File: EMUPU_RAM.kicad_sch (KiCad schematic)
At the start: 22 parts, among them J1 Conn_01x20_Socket, J2 Conn_01x20_Socket, J3 Barrel_Jack_Switch, J4 Conn_01x06_Pin, J5 Conn_01x08_Pin, J6 Conn_01x06_Pin, J7 Conn_01x02_Pin, SW1 SW_SPDT, SW2 SW_SPST, U1 PIC18F57Q43-IPT, U2 HM678127_SOJ32_Arranged

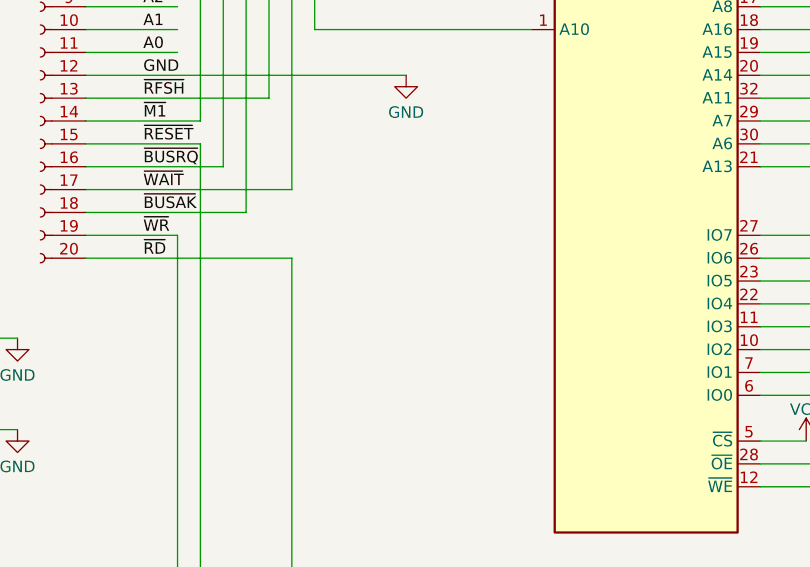
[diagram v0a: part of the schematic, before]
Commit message: Adjusting rule, described in Kosakas book, need some refinements
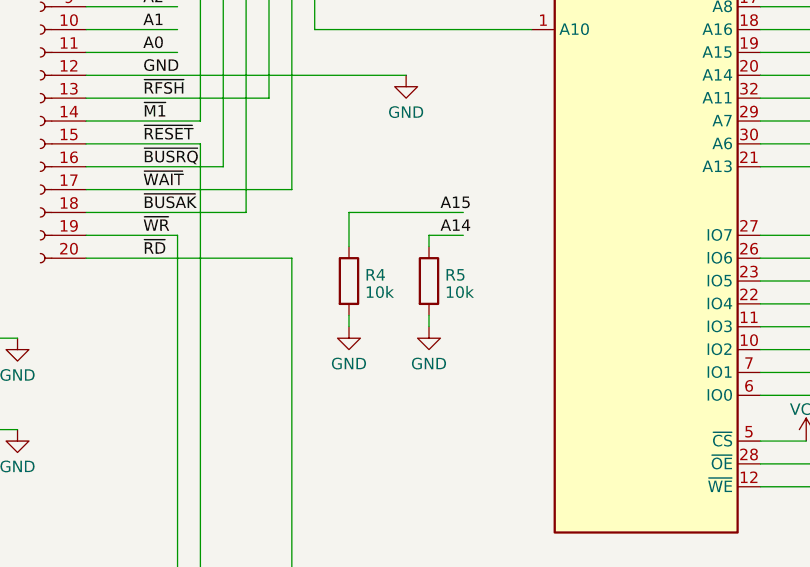
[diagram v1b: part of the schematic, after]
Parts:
- added R4, R5: 10k, Resistor_THT:R_Axial_DIN0204_L3.6mm_D1.6mm_P7.62mm_Horizontal, symbol Device:R
- J4, J6: footprint Connector_PinHeader_2.54mm:PinHeader_1x06_P2.54mm_Horizontal -> 0-local:PinHeader_1x06_P2.54mm_Horizontal_NoFeet
- J5: footprint 0-local:PinHeader_1x08_P2.54mm_Rev_Horizontal -> 0-local:PinHeader_1x08_P2.54mm_Rev_Horizontal_Nofoot
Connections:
- net A14: now also R5.1
- net A15: now also R4.1
- net GND: now also R4.2, R5.2
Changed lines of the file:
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@@
+    (stroke (width 0) (type default))
+  )
+  (wire (pts (xy 101.6 93.98) (xy 114.3 93.98))
     (stroke (width 0) (type default))
   )
@@
     (stroke (width 0) (type default))
   )
+  (wire (pts (xy 110.49 96.52) (xy 110.49 97.79))
+    (stroke (width 0) (type default))
+  )
   (wire (pts (xy 24.13 58.42) (xy 44.45 58.42))
     (stroke (width 0) (type default))
@@
     (stroke (width 0) (type default))
   )
+  (wire (pts (xy 114.3 96.52) (xy 110.49 96.52))
+    (stroke (width 0) (type default))
+  )
   (wire (pts (xy 165.1 124.46) (xy 165.1 144.78))
     (stroke (width 0) (type default))
@@
     (stroke (width 0) (type default))
   )
+  (wire (pts (xy 101.6 105.41) (xy 101.6 106.68))
+    (stroke (width 0) (type default))
+  )
   (wire (pts (xy 72.39 99.06) (xy 95.25 99.06))
     (stroke (width 0) (type default))
@@
     (stroke (width 0) (type default))
   )
+  (wire (pts (xy 101.6 97.79) (xy 101.6 93.98))
+    (stroke (width 0) (type default))
+  )
   (wire (pts (xy 21.59 93.98) (xy 44.45 93.98))
     (stroke (width 0) (type default))
@@
     (stroke (width 0) (type default))
   )
+  (wire (pts (xy 110.49 105.41) (xy 110.49 106.68))
+    (stroke (width 0) (type default))
+  )
   (wire (pts (xy 85.09 30.48) (xy 85.09 83.82))
     (stroke (width 0) (type default))
@@
     (effects (font (size 1.27 1.27)) (justify left bottom))
   )
+  (label "A15" (at 111.76 93.98 0) (fields_autoplaced)
+    (effects (font (size 1.27 1.27)) (justify left bottom))
+  )
   (label "~{BUSRQ}" (at 78.74 88.9 0) (fields_autoplaced)
     (effects (font (size 1.27 1.27)) (justify left bottom))
@@
   )
   (label "CLK" (at 34.29 63.5 0) (fields_autoplaced)
+    (effects (font (size 1.27 1.27)) (justify left bottom))
+  )
+  (label "A14" (at 111.76 96.52 0) (fields_autoplaced)
     (effects (font (size 1.27 1.27)) (justify left bottom))
   )
@@
       (effects (font (size 1.27 1.27)) (justify right))
     )
-    (property "Footprint" "0-local:PinHeader_1x08_P2.54mm_Rev_Horizontal" (at 271.78 149.86 0)
+    (property "Footprint" "0-local:PinHeader_1x08_P2.54mm_Rev_Horizontal_Nofoot" (at 271.78 149.86 0)
       (effects (font (size 1.27 1.27)) hide)
     )
@@
     )
   )
+  (symbol (lib_id "power:GND") (at 101.6 106.68 0) (unit 1)
+    (in_bom yes) (on_board yes) (dnp no) (fields_autoplaced)
+    (property "Reference" "#PWR027" (at 101.6 113.03 0)
+      (effects (font (size 1.27 1.27)) hide)
+    )
+    (property "Value" "GND" (at 101.6 110.8155 0)
+      (effects (font (size 1.27 1.27)))
+    )
+    (property "Footprint" "" (at 101.6 106.68 0)
+      (effects (font (size 1.27 1.27)) hide)
+    )
+    (property "Datasheet" "" (at 101.6 106.68 0)
+      (effects (font (size 1.27 1.27)) hide)
+    )
+    (pin "1")
+    (instances
+      (project "EMUPU_RAM"
+        (path "/6d2188b2-a6ec-4341-9e2f-19ddbe5554d2"
+          (reference "#PWR027") (unit 1)
+        )
+      )
+    )
+  )
   (symbol (lib_id "Connector:Conn_01x06_Pin") (at 271.78 76.2 0) (mirror y) (unit 1)
     (in_bom yes) (on_board yes) (dnp no)
@@
       (effects (font (size 1.27 1.27)) (justify right))
     )
-    (property "Footprint" "Connector_PinHeader_2.54mm:PinHeader_1x06_P2.54mm_Horizontal" (at 271.78 76.2 0)
+    (property "Footprint" "0-local:PinHeader_1x06_P2.54mm_Horizontal_NoFeet" (at 271.78 76.2 0)
       (effects (font (size 1.27 1.27)) hide)
     )
@@
         (path "/6d2188b2-a6ec-4341-9e2f-19ddbe5554d2"
           (reference "C3") (unit 1)
+        )
+      )
+    )
+  )
+  (symbol (lib_id "Device:R") (at 110.49 101.6 0) (unit 1)
+    (in_bom yes) (on_board yes) (dnp no) (fields_autoplaced)
+    (property "Reference" "R5" (at 112.268 100.9563 0)
+      (effects (font (size 1.27 1.27)) (justify left))
+    )
+    (property "Value" "10k" (at 112.268 102.8773 0)
+      (effects (font (size 1.27 1.27)) (justify left))
+    )
+    (property "Footprint" "Resistor_THT:R_Axial_DIN0204_L3.6mm_D1.6mm_P7.62mm_Horizontal" (at 108.712 101.6 90)
+      (effects (font (size 1.27 1.27)) hide)
+    )
+    (property "Datasheet" "~" (at 110.49 101.6 0)
+      (effects (font (size 1.27 1.27)) hide)
+    )
+    (pin "1")
+    (pin "2")
+    (instances
+      (project "EMUPU_RAM"
+        (path "/6d2188b2-a6ec-4341-9e2f-19ddbe5554d2"
+          (reference "R5") (unit 1)
         )
       )
@@
     )
   )
+  (symbol (lib_id "Device:R") (at 101.6 101.6 0) (unit 1)
+    (in_bom yes) (on_board yes) (dnp no) (fields_autoplaced)
+    (property "Reference" "R4" (at 103.378 100.9563 0)
+      (effects (font (size 1.27 1.27)) (justify left))
+    )
+    (property "Value" "10k" (at 103.378 102.8773 0)
+      (effects (font (size 1.27 1.27)) (justify left))
+    )
+    (property "Footprint" "Resistor_THT:R_Axial_DIN0204_L3.6mm_D1.6mm_P7.62mm_Horizontal" (at 99.822 101.6 90)
+      (effects (font (size 1.27 1.27)) hide)
+    )
+    (property "Datasheet" "~" (at 101.6 101.6 0)
+      (effects (font (size 1.27 1.27)) hide)
+    )
+    (pin "1")
+    (pin "2")
+    (instances
+      (project "EMUPU_RAM"
+        (path "/6d2188b2-a6ec-4341-9e2f-19ddbe5554d2"
+          (reference "R4") (unit 1)
+        )
+      )
+    )
+  )
   (symbol (lib_id "power:GND") (at 64.77 107.95 0) (unit 1)
     (in_bom yes) (on_board yes) (dnp no) (fields_autoplaced)
@@
     )
   )
+  (symbol (lib_id "power:GND") (at 110.49 106.68 0) (unit 1)
+    (in_bom yes) (on_board yes) (dnp no) (fields_autoplaced)
+    (property "Reference" "#PWR028" (at 110.49 113.03 0)
+      (effects (font (size 1.27 1.27)) hide)
+    )
+    (property "Value" "GND" (at 110.49 110.8155 0)
+      (effects (font (size 1.27 1.27)))
+    )
+    (property "Footprint" "" (at 110.49 106.68 0)
+      (effects (font (size 1.27 1.27)) hide)
+    )
+    (property "Datasheet" "" (at 110.49 106.68 0)
+      (effects (font (size 1.27 1.27)) hide)
+    )
+    (pin "1")
+    (instances
+      (project "EMUPU_RAM"
+        (path "/6d2188b2-a6ec-4341-9e2f-19ddbe5554d2"
+          (reference "#PWR028") (unit 1)
+        )
+      )
+    )
+  )
   (symbol (lib_id "power:GND") (at 118.11 64.77 0) (unit 1)
     (in_bom yes) (on_board yes) (dnp no) (fields_autoplaced)
@@
       (effects (font (size 1.27 1.27)) (justify right))
     )
-    (property "Footprint" "Connector_PinHeader_2.54mm:PinHeader_1x06_P2.54mm_Horizontal" (at 271.78 111.76 0)
-      (effects (font (size 1.27 1.27)) hide)
-    )
+    (property "Footprint" "0-local:PinHeader_1x06_P2.54mm_Horizontal_NoFeet" (at 271.78 111.76 0)
+      (effects (font (size 1.27 1.27)) hide)
+    )

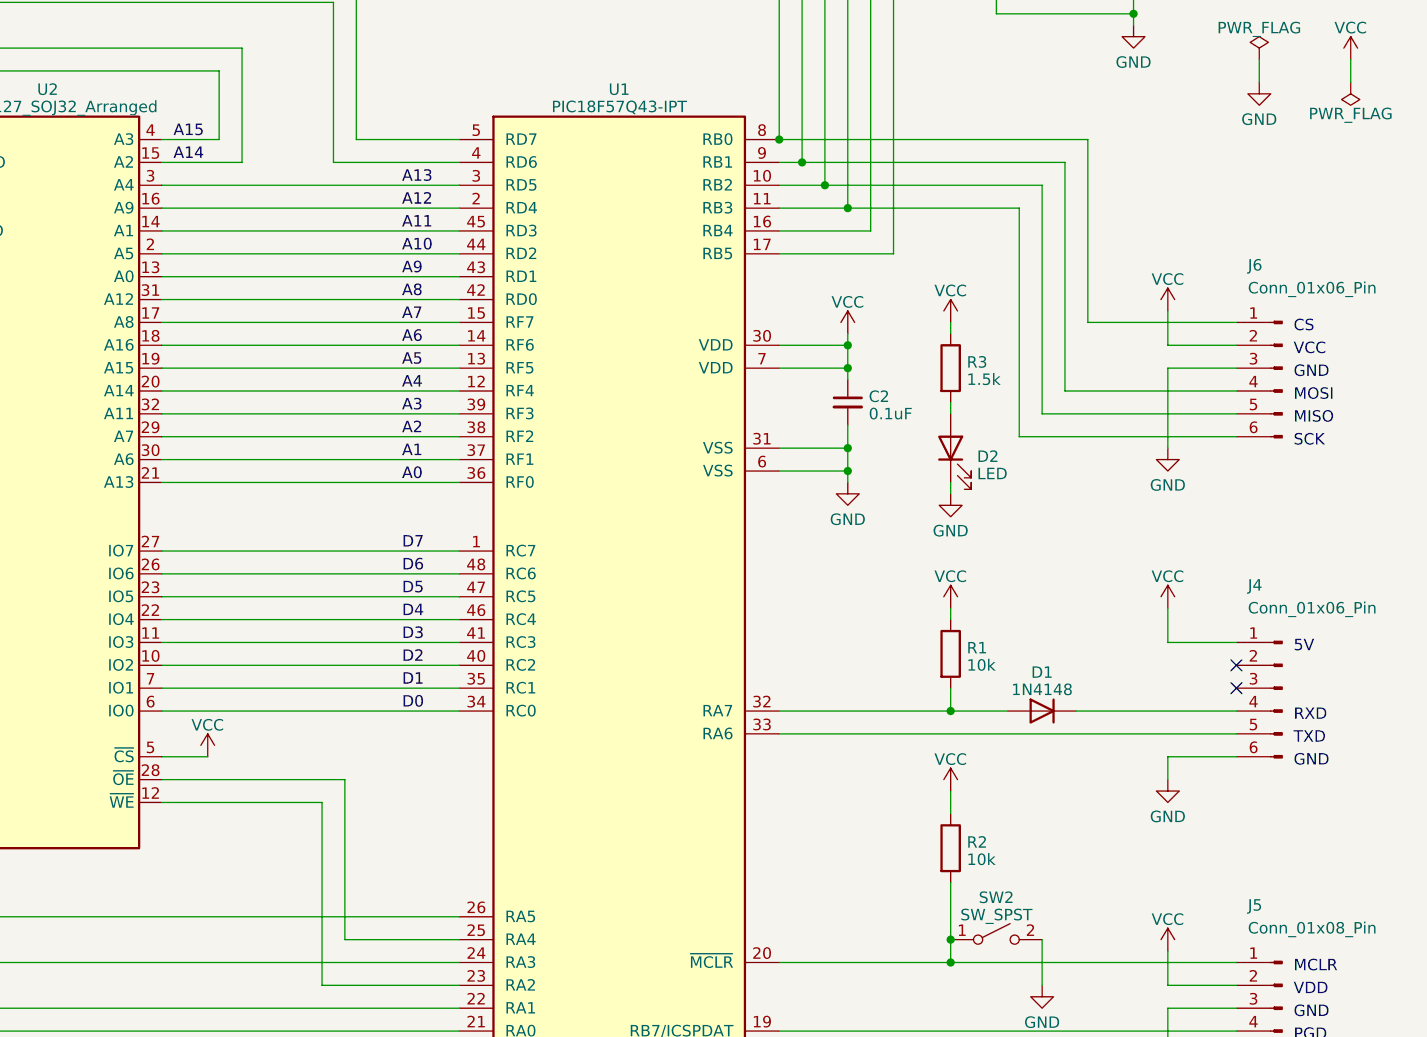
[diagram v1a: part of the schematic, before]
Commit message: Add Z80 label, RBx jumpers, garbers, ZIP
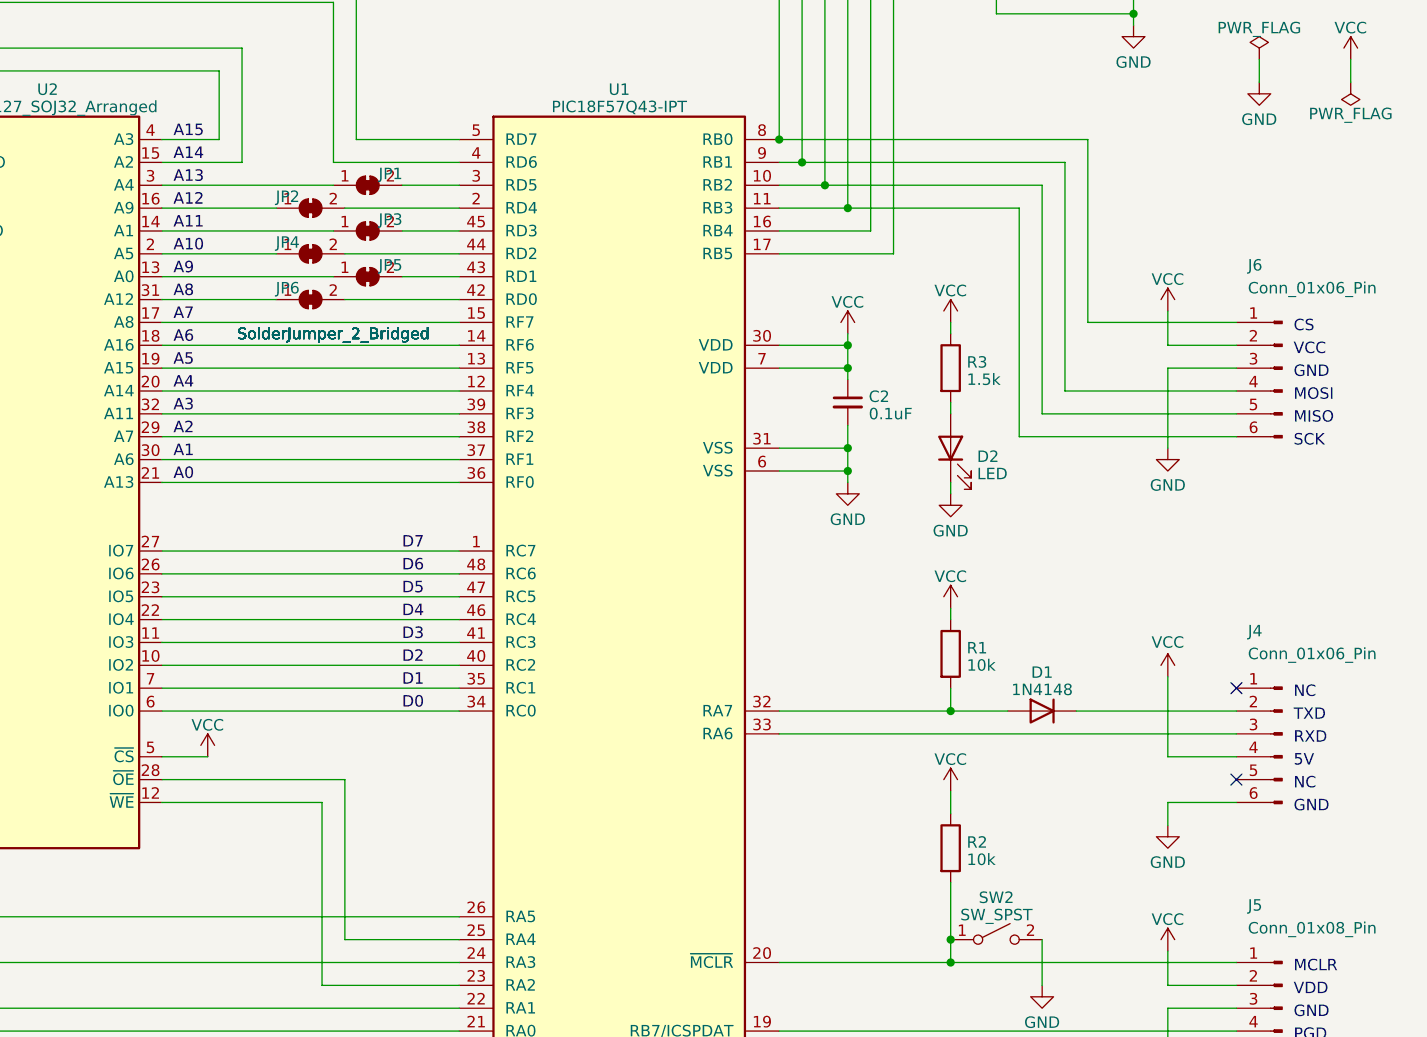
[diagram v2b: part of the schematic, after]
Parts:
- added JP1, JP2, JP3, JP4, JP5, JP6: SolderJumper_2_Bridged, Jumper:SolderJumper-2_P1.3mm_Bridged_RoundedPad1.0x1.5mm, symbol Jumper:SolderJumper_2_Bridged
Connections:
- net A10: now also JP4.1 (A); no longer U1.44 (RD2)
- net A11: now also JP3.1 (A); no longer U1.45 (RD3)
- net A12: now also JP2.1 (A); no longer U1.2 (RD4)
- net A13: now also JP1.1 (A); no longer U1.3 (RD5)
- net A8: now also JP6.1 (A); no longer U1.42 (RD0)
- net A9: now also JP5.1 (A); no longer U1.43 (RD1)
- net VCC: now also J4.4 (Pin_4); no longer J4.1 (Pin_1)
- net at D1.1 (K): now also J4.2 (Pin_2); no longer J4.4 (Pin_4)
- net at U1.33 (RA6): now also J4.3 (Pin_3); no longer J4.5 (Pin_5)
- new net: JP3.2 (B), U1.45 (RD3)
- new net: JP6.2 (B), U1.42 (RD0)
- new net: JP1.2 (B), U1.3 (RD5)
- new net: JP5.2 (B), U1.43 (RD1)
- new net: JP2.2 (B), U1.2 (RD4)
- new net: JP4.2 (B), U1.44 (RD2)
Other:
- moved on the sheet: J4
